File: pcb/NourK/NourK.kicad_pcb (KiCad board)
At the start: 4 copper layers, 414.5 x 281.2 mm, 187 parts, among them IC1 IS31FL3733B-QFLS4-TR, J1 SJ-435107RS, J2 Conn_ARM_JTAG_SWD_10, J3 USB_C_Receptacle_USB2.0, J4 USB_C_Receptacle_USB2.0, J5 SJ-435107RS, SW1 SW_SPDT, SW10 LAYER, SW11 I, SW12 K, SW13 ,, SW14 LAYER, SW15 O, SW16 L, SW17 ., SW18 LAYER, SW19 P, SW2 SW_SPST_G, SW20 ;, SW21 /, SW22 RCTRL, SW23 [, SW24 ', SW25 RSHIFT, SW26 ], SW27 ENTER, SW3 Y, SW30 ESCAPE, SW31 OSKEY, SW32 TAB, SW33 GRAVE, SW34 LEFT_SHIFT, SW35 Q, SW36 A, SW37 Z, SW38 LEFT_CTRL, SW39 W, SW4 H, SW40 S, SW41 X, SW42 LAYER1, SW43 E, SW44 D, SW45 C, SW46 LAYER2, SW47 R, SW48 F, SW49 V, SW5 N, SW50 LEFT_ALT, SW51 T, SW52 G, SW53 B, SW54 SPACE, SW6 SPACE, SW7 U, SW8 J, SW9 M, U1 STM32L082CZYx, U2 AP2112K-3.3, U3 NourK_Core, U4 NourK_Core, U5 NourK_Core, Y1 32.768KHz, Y2 8MHz

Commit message: Complete wiring
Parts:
- added REF**: MountingHole_2.2mm_M2, MountingHole:MountingHole_2.2mm_M2, F.Cu at (63.5, 212.8)
- added REF**: MountingHole, MountingHole:MountingHole_2.2mm_M2, F.Cu at (72.4, 42.2)
- added REF**: MountingHole, MountingHole:MountingHole_2.2mm_M2, F.Cu at (88.5, 42.2)
- added REF**: MountingHole_2.2mm_M2, MountingHole:MountingHole_2.2mm_M2, F.Cu at (158.5, 120.8)
- moved D1 208.0 mm to (139.0, 82.8)
- moved D10 208.0 mm to (168.0, 116.5)
- moved D11 208.0 mm to (168.0, 135.5)
- moved D12 208.0 mm to (171.5, 154.5)
- moved D13 208.0 mm to (149.0, 95.5)
- moved D14 208.0 mm to (149.0, 114.5)
- moved D15 208.0 mm to (149.0, 133.5)
- moved D16 208.0 mm to (149.0, 152.5)
- moved D17 208.0 mm to (130.0, 89.5)
- moved D18 208.0 mm to (130.0, 108.5)
- moved D19 208.0 mm to (130.0, 127.5)
- moved D2 208.0 mm to (139.0, 101.8)
- moved D20 208.0 mm to (130.0, 146.5)
- moved D21 208.0 mm to (111.0, 92.5)
- moved D22 208.0 mm to (111.0, 111.5)
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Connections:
- D1 pad 3: /rhs/RHS Keys/KEY.ROW10 -> /rhs/RHS Keys/KEY.ROW8
- D1 pad 6: /rhs/RHS Keys/KEY.ROW10 -> /rhs/RHS Keys/KEY.ROW8
- D1 pad 7: /rhs/RHS Keys/KEY.ROW10 -> /rhs/RHS Keys/KEY.ROW8
- D1 pad 8: /rhs/RHS Keys/KEY.ROW10 -> /rhs/RHS Keys/KEY.ROW8
- D5 pad 3: /rhs/RHS Keys/KEY.ROW10 -> /rhs/RHS Keys/KEY.ROW8
- D5 pad 6: /rhs/RHS Keys/KEY.ROW10 -> /rhs/RHS Keys/KEY.ROW8
- D5 pad 7: /rhs/RHS Keys/KEY.ROW10 -> /rhs/RHS Keys/KEY.ROW8
- D5 pad 8: /rhs/RHS Keys/KEY.ROW10 -> /rhs/RHS Keys/KEY.ROW8
- IC1 pad 10: /core/LED.SW_RED1 -> /core/LED.SW_RED2
- IC1 pad 11: /core/LED.SW_BLUE1 -> /core/LED.SW_BLUE2
- IC1 pad 13: /core/LED.SW_GREEN2 -> /core/LED.SW_GREEN1
- IC1 pad 14: /core/LED.SW_RED2 -> /core/LED.SW_RED1
- IC1 pad 15: /core/LED.SW_BLUE2 -> /core/LED.SW_BLUE1
- IC1 pad 2: /core/LED.SW_GREEN3 -> /core/LED.SW_GREEN4
- IC1 pad 3: /core/LED.SW_RED3 -> /core/LED.SW_RED4
- IC1 pad 4: /core/LED.SW_BLUE3 -> /core/LED.SW_BLUE4
- IC1 pad 6: /core/LED.SW_GREEN4 -> /core/LED.SW_GREEN3
- IC1 pad 7: /core/LED.SW_RED4 -> /core/LED.SW_RED3
- IC1 pad 8: /core/LED.SW_BLUE4 -> /core/LED.SW_BLUE3
- IC1 pad 9: /core/LED.SW_GREEN1 -> /core/LED.SW_GREEN2
- J1 pad 2: VCC -> Net-(J1-Pad2)
- J1 pad 5: unconnected-(J1-Pad5) -> Net-(J1-Pad2)
- J1 pad 6: unconnected-(J1-Pad6) -> VCC
- J5 pad 2: VCC -> Net-(J5-Pad2)
- J5 pad 5: unconnected-(J5-Pad5) -> Net-(J5-Pad2)
- J5 pad 6: unconnected-(J5-Pad6) -> VCC
- U4 pad 19: /core/LED.SW_RED4 -> /core/LED.SW_GREEN4
- U4 pad 30: /core/LED.SW_BLUE4 -> /core/LED.SW_RED4
- U4 pad 31: /core/LED.SW_GREEN4 -> /core/LED.SW_BLUE4
- U4 pad 41: /core/LED.SW_RED2 -> /core/LED.SW_RED1
- U4 pad 42: /core/LED.SW_GREEN1 -> /core/LED.SW_GREEN2
- U4 pad 43: /core/LED.SW_BLUE1 -> /core/LED.SW_BLUE2
- U4 pad 6: /core/LED.SW_RED1 -> /core/LED.SW_RED2
- U4 pad 7: /core/LED.SW_GREEN2 -> /core/LED.SW_GREEN1
- U4 pad 8: /core/LED.SW_BLUE2 -> /core/LED.SW_BLUE1
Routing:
- net /rhs/RHS Keys/KEY.ROW8: track 0.00 -> 109.9 mm
- net /rhs/RHS Keys/KEY.ROW10: track 108.3 -> 0.00 mm
- net /core/USART.RX: track 117.2 -> 63.6 mm
- net /lhs/LHS LEDs/LED.CS_COL7: track 103.7 -> 77.7 mm, vias 1 -> 0
- net /lhs/LHS LEDs/LED.CS_COL4: track 163.5 -> 140.5 mm
- net /lhs/LHS LEDs/LED.CS_COL5: track 141.2 -> 118.5 mm
- net /lhs/LHS LEDs/LED.CS_COL3: track 181.3 -> 159.1 mm
- net /lhs/LHS LEDs/LED.CS_COL6: track 121.9 -> 100.0 mm
- net /lhs/LHS Keys/KEY.COL6: track 136.7 -> 116.0 mm, vias 0 -> 1
- net /rhs/RHS LEDs/LED.CS_COL13: track 188.9 -> 208.5 mm
- net /lhs/LHS LEDs/LED.CS_COL2: track 176.6 -> 159.7 mm
- net VCC: track 46.8 -> 32.1 mm
- net /rhs/RHS Keys/KEY.COL2: track 95.9 -> 81.6 mm
- net /rhs/RHS LEDs/LED.SW_GREEN1: track 188.6 -> 202.6 mm
- net /core/USART.TX: track 80.8 -> 67.3 mm, vias 2 -> 3
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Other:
- board size 414.5 x 281.2 mm -> 145.4 x 226.5 mm
- board text added: "(A) 4 layer PCB, 2x"
- board text added: "(B) 2 layer PCB, 1x"
- board text added: "(C) 2 layer PCB, 1x"
- board text added: "Nour Valkyrie Core v0.1"
- board text added: "Nour Valkyrie Left Wing v0.1"
- board text added: "Nour Valkyrie Right Wing v0.1"

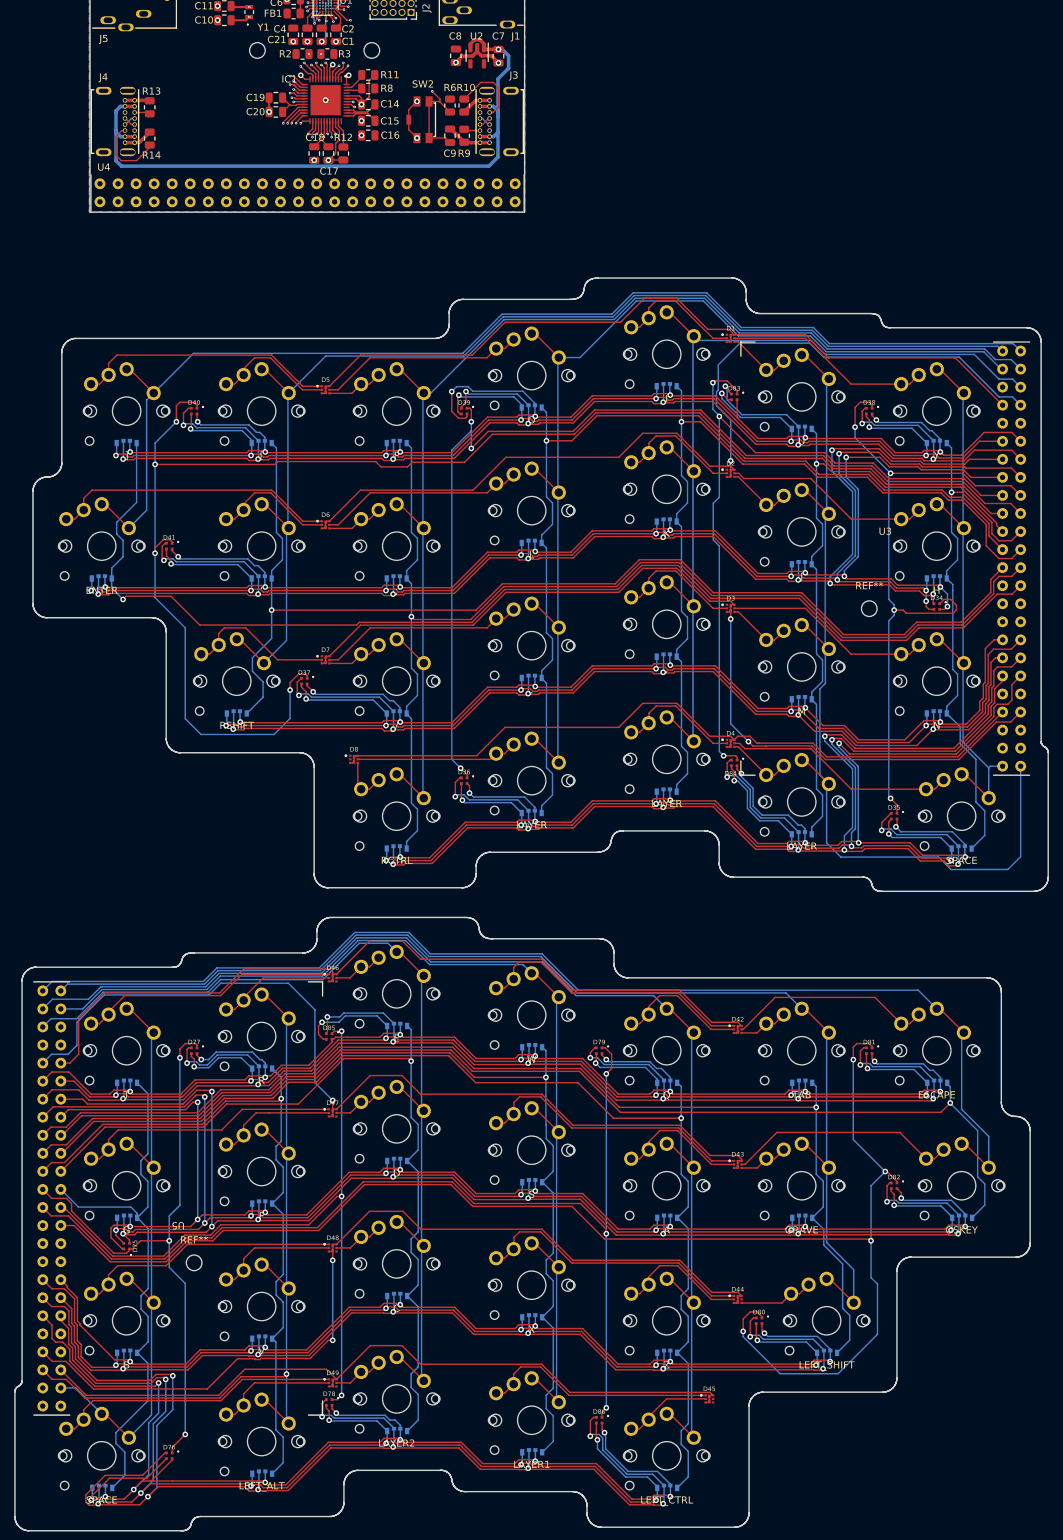
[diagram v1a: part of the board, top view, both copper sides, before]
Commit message: Add mounting holes
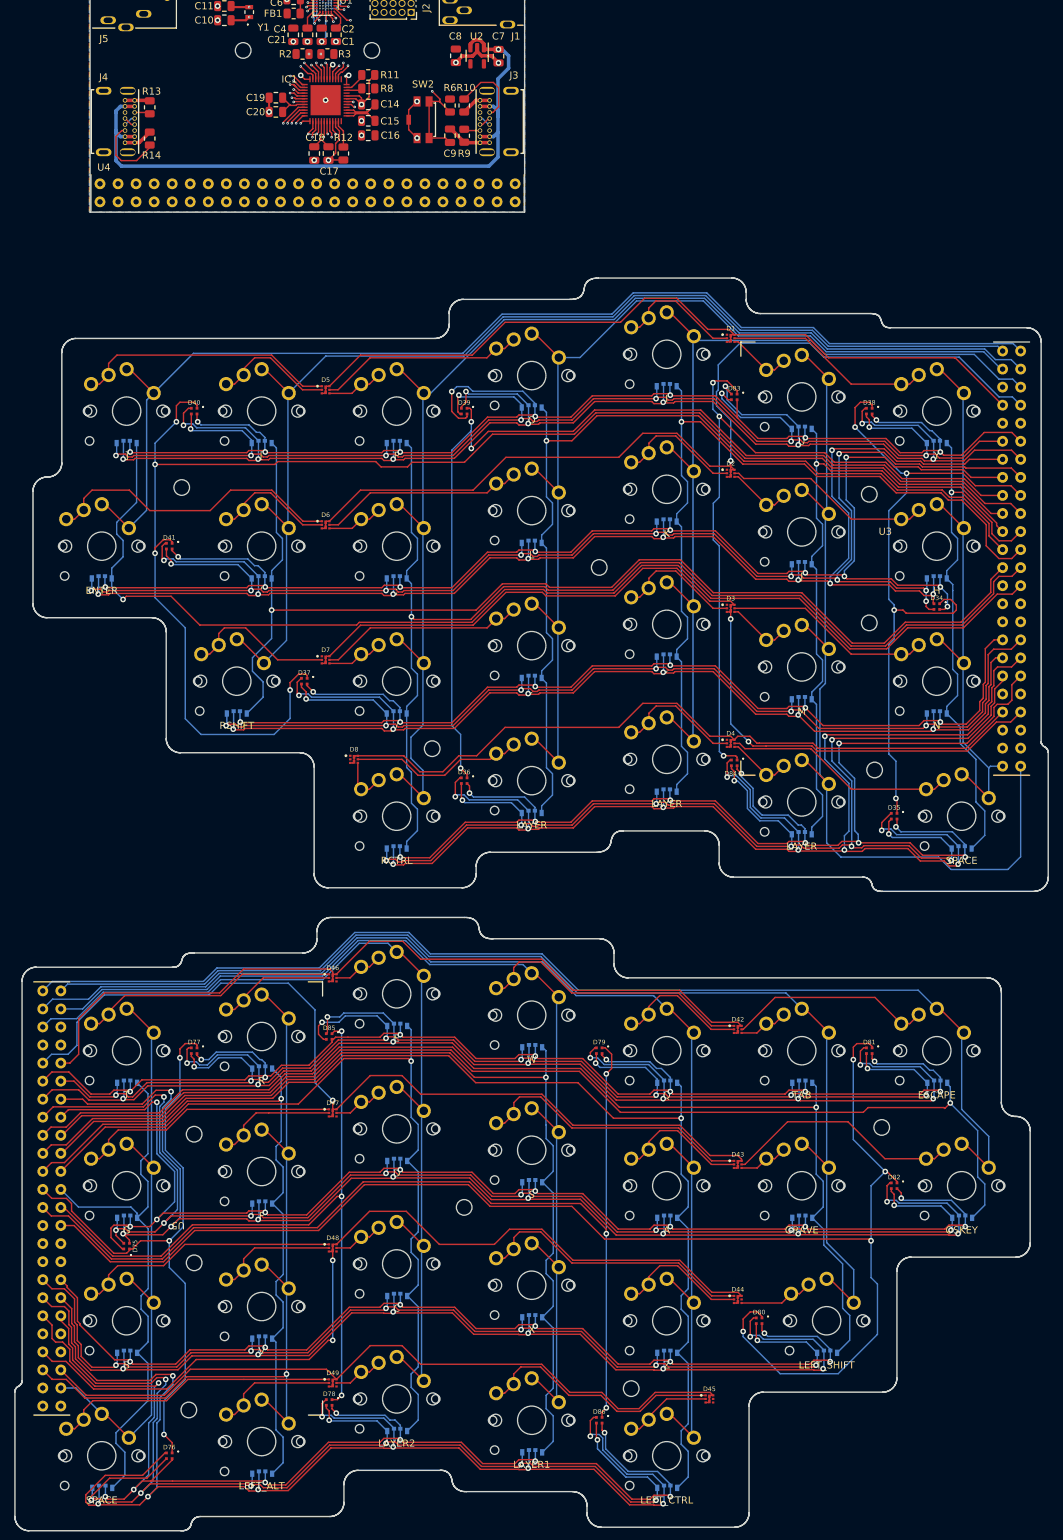
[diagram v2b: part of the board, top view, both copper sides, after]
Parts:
- added REF**: MountingHole_2.2mm_M2, MountingHole:MountingHole_2.2mm_M2, F.Cu at (120.5, 115.0)
- added REF**: MountingHole_2.2mm_M2, MountingHole:MountingHole_2.2mm_M2, F.Cu at (101.5, 205.1)
- added REF**: MountingHole_2.2mm_M2, MountingHole:MountingHole_2.2mm_M2, F.Cu at (63.5, 194.8)
- added REF**: MountingHole_2.2mm_M2, MountingHole:MountingHole_2.2mm_M2, F.Cu at (158.5, 104.7)
- added REF**: MountingHole_2.2mm_M2, MountingHole:MountingHole_2.2mm_M2, F.Cu at (125.0, 230.6)
- added REF**: MountingHole_2.2mm_M2, MountingHole:MountingHole_2.2mm_M2, F.Cu at (62.8, 233.6)
- added REF**: MountingHole_2.2mm_M2, MountingHole:MountingHole_2.2mm_M2, F.Cu at (97.0, 140.5)
- added REF**: MountingHole_2.2mm_M2, MountingHole:MountingHole_2.2mm_M2, F.Cu at (160.2, 193.8)
- added REF**: MountingHole_2.2mm_M2, MountingHole:MountingHole_2.2mm_M2, F.Cu at (159.2, 143.5)
- added REF**: MountingHole_2.2mm_M2, MountingHole:MountingHole_2.2mm_M2, F.Cu at (61.8, 103.8)
- moved REF** 2.00 mm to (158.5, 122.8)
- moved REF** 2.00 mm to (70.4, 42.2)
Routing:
- net /lhs/LHS LEDs/LED.SW_RED2: track 194.7 -> 191.0 mm
- net /lhs/LHS LEDs/LED.SW_BLUE2: track 192.7 -> 189.0 mm
- net /lhs/LHS LEDs/LED.SW_GREEN2: track 200.6 -> 197.1 mm
- net /lhs/LHS LEDs/LED.CS_COL8: track 85.3 -> 88.4 mm
- net Net-(D6-Pad1): track 40.4 -> 42.8 mm
- net /rhs/RHS LEDs/LED.SW_GREEN1: track 202.6 -> 200.6 mm
- net /rhs/RHS LEDs/LED.SW_RED1: track 183.4 -> 181.5 mm
- net /lhs/LHS Keys/KEY.ROW10: track 104.0 -> 105.9 mm
- net Net-(D8-Pad5): track 22.8 -> 24.7 mm
- net Net-(D45-Pad1): track 33.5 -> 35.4 mm
- net /rhs/RHS LEDs/LED.SW_RED2: track 156.8 -> 155.1 mm
- net /rhs/RHS LEDs/LED.SW_BLUE2: track 151.5 -> 149.8 mm
- net /rhs/RHS LEDs/LED.SW_GREEN2: track 158.8 -> 157.2 mm
- net /lhs/LHS Keys/KEY.ROW9: track 126.2 -> 127.8 mm
- net /rhs/RHS LEDs/LED.CS_COL8: track 159.6 -> 161.0 mm
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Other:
- board text added: "(A) 61x41mm 4 layer PCB, 2x"
- board text added: "(B) 142x86mm 2 layer PCB, 1x"
- board text added: "(C) 142x86mm 2 layer PCB, 1x"
- board text removed: "(A) 4 layer PCB, 2x"
- board text removed: "(B) 2 layer PCB, 1x"
- board text removed: "(C) 2 layer PCB, 1x"
